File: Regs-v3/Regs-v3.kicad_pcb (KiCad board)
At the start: 2 copper layers, 149.9 x 99.1 mm, 16 parts, among them U1 REG_CNT, U10 REG_CNT, U2 REG_CNT, U3 REG_CNT, U4 REG_CNT, U5 REG_CNT, U6 REG_CNT, U7 REG_CNT, U8 REG_CNT, U9 REG_CNT

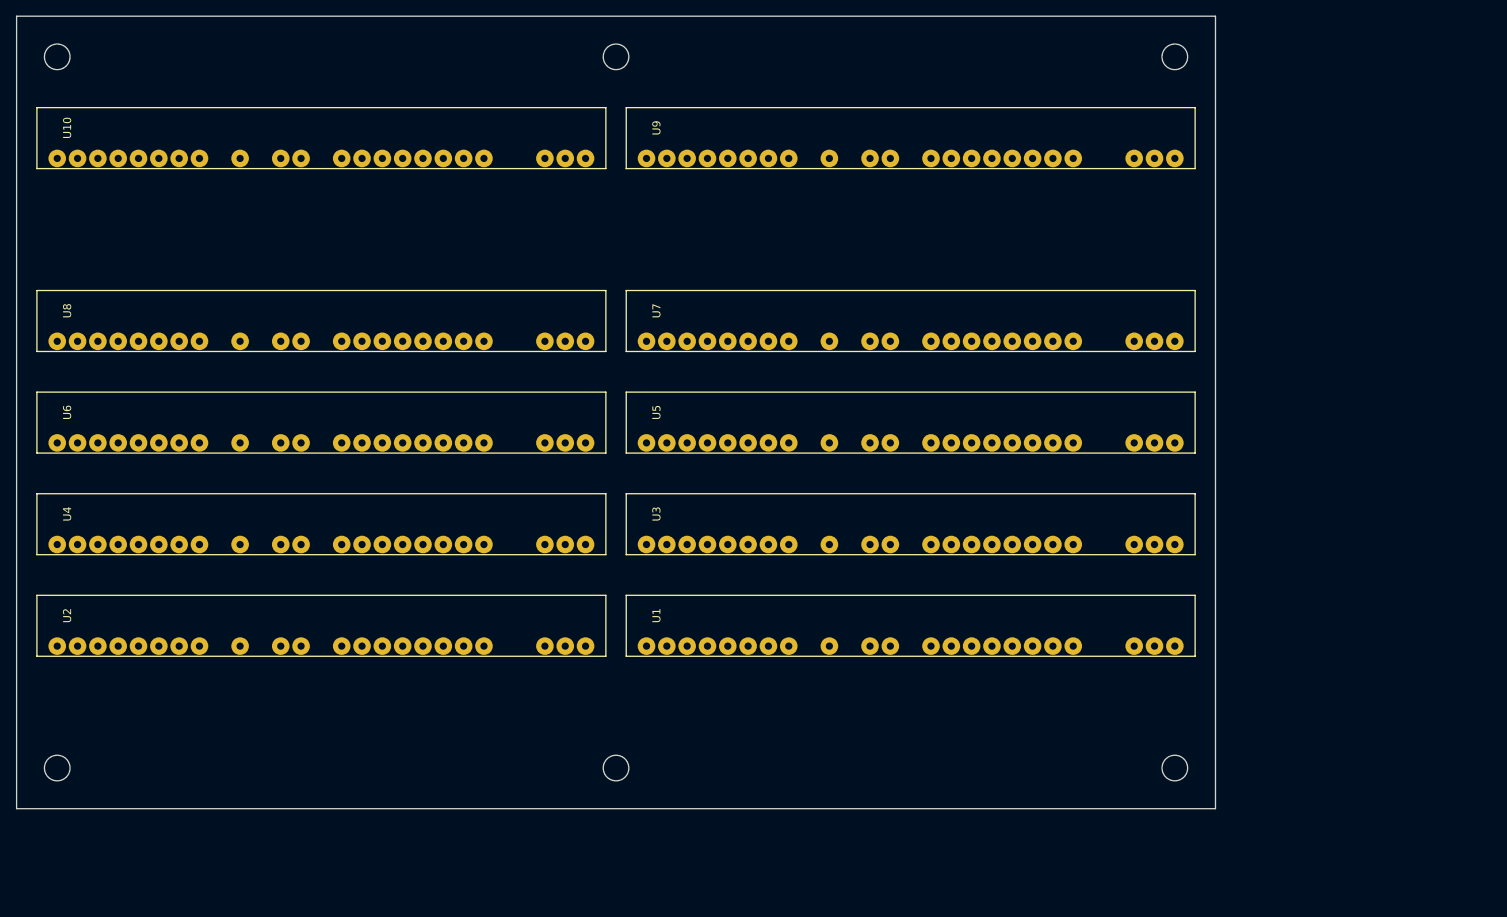
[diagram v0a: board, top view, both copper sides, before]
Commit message: Regs pcb in work
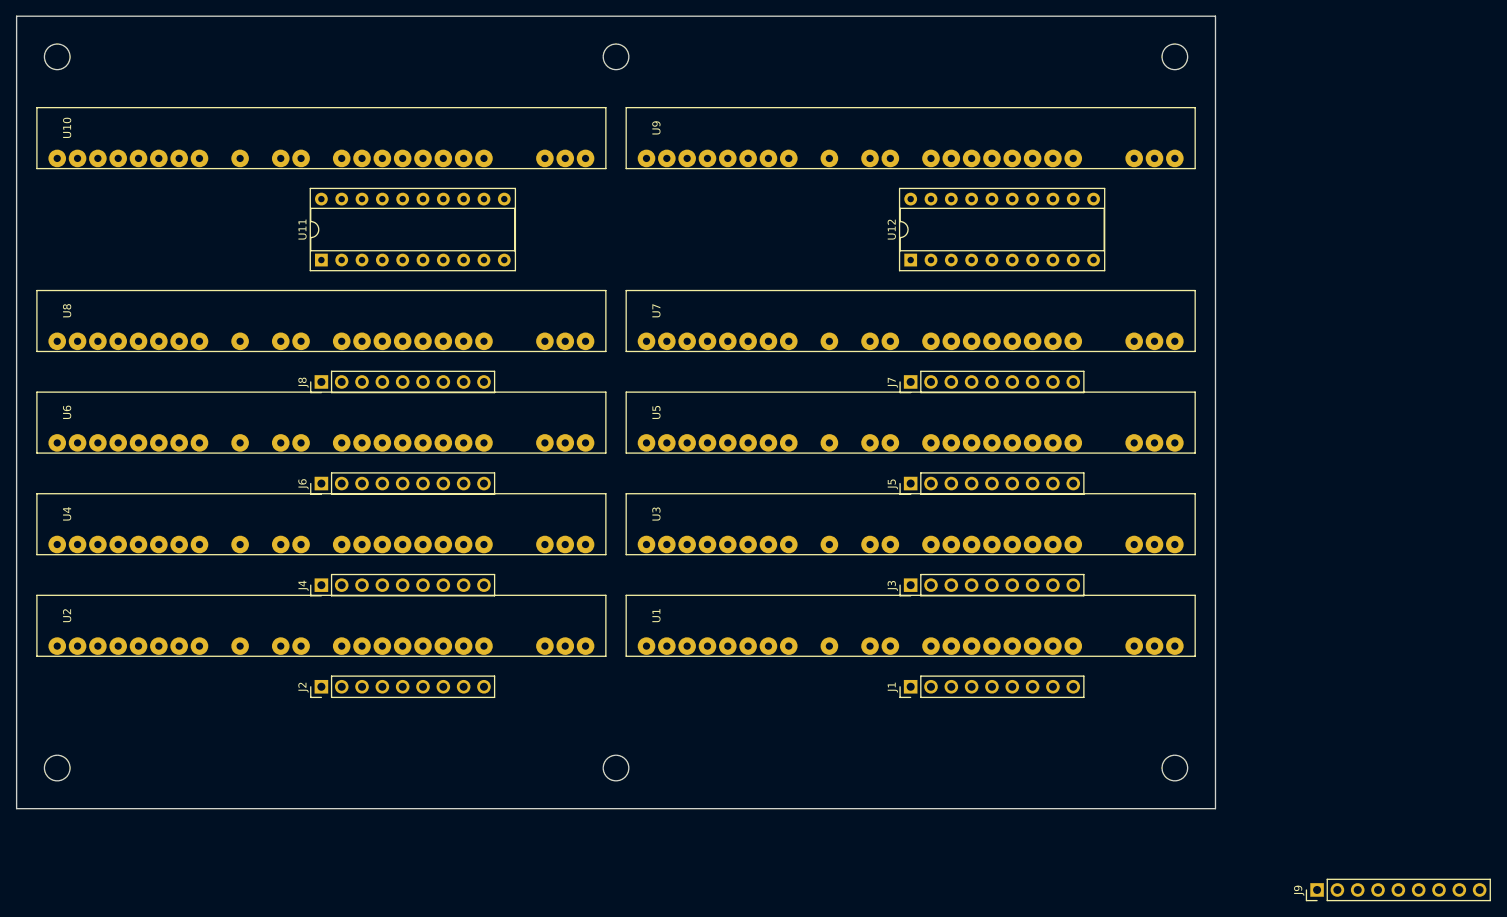
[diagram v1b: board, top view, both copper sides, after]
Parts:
- added J1: Conn_01x09_Male, Connector_PinHeader_2.54mm:PinHeader_1x09_P2.54mm_Vertical, F.Cu at (127.0, 99.1)
- added J2: Conn_01x09_Male, Connector_PinHeader_2.54mm:PinHeader_1x09_P2.54mm_Vertical, F.Cu at (53.3, 99.1)
- added J3: Conn_01x09_Male, Connector_PinHeader_2.54mm:PinHeader_1x09_P2.54mm_Vertical, F.Cu at (127.0, 86.4)
- added J4: Conn_01x09_Male, Connector_PinHeader_2.54mm:PinHeader_1x09_P2.54mm_Vertical, F.Cu at (53.3, 86.4)
- added J5: Conn_01x09_Male, Connector_PinHeader_2.54mm:PinHeader_1x09_P2.54mm_Vertical, F.Cu at (127.0, 73.7)
- added J6: Conn_01x09_Male, Connector_PinHeader_2.54mm:PinHeader_1x09_P2.54mm_Vertical, F.Cu at (53.3, 73.7)
- added J7: Conn_01x09_Male, Connector_PinHeader_2.54mm:PinHeader_1x09_P2.54mm_Vertical, F.Cu at (127.0, 61.0)
- added J8: Conn_01x09_Male, Connector_PinHeader_2.54mm:PinHeader_1x09_P2.54mm_Vertical, F.Cu at (53.3, 61.0)
- added J9: Conn_01x09_Male, Connector_PinHeader_2.54mm:PinHeader_1x09_P2.54mm_Vertical, F.Cu at (177.8, 124.5)
- added U11: 74HC245, Package_DIP:DIP-20_W7.62mm_Socket, F.Cu at (53.3, 45.7)
- added U12: 74HC245, Package_DIP:DIP-20_W7.62mm_Socket, F.Cu at (127.0, 45.7)
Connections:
- net Net-(U10-Pad12) renamed /SPH.0
- net Net-(U10-Pad13) renamed /SPH.1
- net Net-(U10-Pad14) renamed /SPH.2
- net Net-(U10-Pad15) renamed /SPH.3
- net Net-(U10-Pad16) renamed /SPH.4
- net Net-(U10-Pad17) renamed /SPH.5
- net Net-(U10-Pad18) renamed /SPH.6
- net Net-(U10-Pad19) renamed /SPH.7
- net Net-(U9-Pad12) renamed /SPL.0
- net Net-(U9-Pad13) renamed /SPL.1
- net Net-(U9-Pad14) renamed /SPL.2
- net Net-(U9-Pad15) renamed /SPL.3
- net Net-(U9-Pad16) renamed /SPL.4
- net Net-(U9-Pad17) renamed /SPL.5
- net Net-(U9-Pad18) renamed /SPL.6
- net Net-(U9-Pad19) renamed /SPL.7
- U1 pad 10: Net-(U1-Pad10) -> GND
- U1 pad 12: Net-(U1-Pad12) -> /R0.0
- U1 pad 13: Net-(U1-Pad13) -> /R0.1
- U1 pad 14: Net-(U1-Pad14) -> /R0.2
- U1 pad 15: Net-(U1-Pad15) -> /R0.3
- U1 pad 16: Net-(U1-Pad16) -> /R0.4
- U1 pad 17: Net-(U1-Pad17) -> /R0.5
- U1 pad 18: Net-(U1-Pad18) -> /R0.6
- U1 pad 19: Net-(U1-Pad19) -> /R0.7
- U10 pad 10: Net-(U10-Pad10) -> GND
- U2 pad 10: Net-(U2-Pad10) -> GND
- U2 pad 12: Net-(U2-Pad12) -> /R1.0
- U2 pad 13: Net-(U2-Pad13) -> /R1.1
- U2 pad 14: Net-(U2-Pad14) -> /R1.2
- U2 pad 15: Net-(U2-Pad15) -> /R1.3
- U2 pad 16: Net-(U2-Pad16) -> /R1.4
- U2 pad 17: Net-(U2-Pad17) -> /R1.5
- U2 pad 18: Net-(U2-Pad18) -> /R1.6
- U2 pad 19: Net-(U2-Pad19) -> /R1.7
- U3 pad 10: Net-(U3-Pad10) -> GND
- U3 pad 12: Net-(U3-Pad12) -> /R2.0
- U3 pad 13: Net-(U3-Pad13) -> /R2.1
- U3 pad 14: Net-(U3-Pad14) -> /R2.2
- U3 pad 15: Net-(U3-Pad15) -> /R2.3
- U3 pad 16: Net-(U3-Pad16) -> /R2.4
- U3 pad 17: Net-(U3-Pad17) -> /R2.5
- U3 pad 18: Net-(U3-Pad18) -> /R2.6
- U3 pad 19: Net-(U3-Pad19) -> /R2.7
- U4 pad 10: Net-(U4-Pad10) -> GND
- U4 pad 12: Net-(U4-Pad12) -> /R3.0
- U4 pad 13: Net-(U4-Pad13) -> /R3.1
- U4 pad 14: Net-(U4-Pad14) -> /R3.2
- U4 pad 15: Net-(U4-Pad15) -> /R3.3
- U4 pad 16: Net-(U4-Pad16) -> /R3.4
- U4 pad 17: Net-(U4-Pad17) -> /R3.5
- U4 pad 18: Net-(U4-Pad18) -> /R3.6
- U4 pad 19: Net-(U4-Pad19) -> /R3.7
- U5 pad 10: Net-(U5-Pad10) -> GND
- U5 pad 12: Net-(U5-Pad12) -> /R4.0
- U5 pad 13: Net-(U5-Pad13) -> /R4.1
- U5 pad 14: Net-(U5-Pad14) -> /R4.2
- U5 pad 15: Net-(U5-Pad15) -> /R4.3
- U5 pad 16: Net-(U5-Pad16) -> /R4.4
- U5 pad 17: Net-(U5-Pad17) -> /R4.5
- U5 pad 18: Net-(U5-Pad18) -> /R4.6
- U5 pad 19: Net-(U5-Pad19) -> /R4.7
- U6 pad 10: Net-(U6-Pad10) -> GND
- U6 pad 12: Net-(U6-Pad12) -> /R5.0
- U6 pad 13: Net-(U6-Pad13) -> /R5.1
- U6 pad 14: Net-(U6-Pad14) -> /R5.2
- U6 pad 15: Net-(U6-Pad15) -> /R5.3
- U6 pad 16: Net-(U6-Pad16) -> /R5.4
- U6 pad 17: Net-(U6-Pad17) -> /R5.5
- U6 pad 18: Net-(U6-Pad18) -> /R5.6
- U6 pad 19: Net-(U6-Pad19) -> /R5.7
- U7 pad 10: Net-(U7-Pad10) -> GND
- U7 pad 12: Net-(U7-Pad12) -> /R6.0
- U7 pad 13: Net-(U7-Pad13) -> /R6.1
- U7 pad 14: Net-(U7-Pad14) -> /R6.2
- U7 pad 15: Net-(U7-Pad15) -> /R6.3
- U7 pad 16: Net-(U7-Pad16) -> /R6.4
- U7 pad 17: Net-(U7-Pad17) -> /R6.5
- U7 pad 18: Net-(U7-Pad18) -> /R6.6
- U7 pad 19: Net-(U7-Pad19) -> /R6.7
- U8 pad 10: Net-(U8-Pad10) -> GND
- U8 pad 12: Net-(U8-Pad12) -> /R7.0
- U8 pad 13: Net-(U8-Pad13) -> /R7.1
- U8 pad 14: Net-(U8-Pad14) -> /R7.2
- U8 pad 15: Net-(U8-Pad15) -> /R7.3
- U8 pad 16: Net-(U8-Pad16) -> /R7.4
- U8 pad 17: Net-(U8-Pad17) -> /R7.5
- U8 pad 18: Net-(U8-Pad18) -> /R7.6
- U8 pad 19: Net-(U8-Pad19) -> /R7.7
- U9 pad 10: Net-(U9-Pad10) -> GND

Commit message: Regs pcb in work
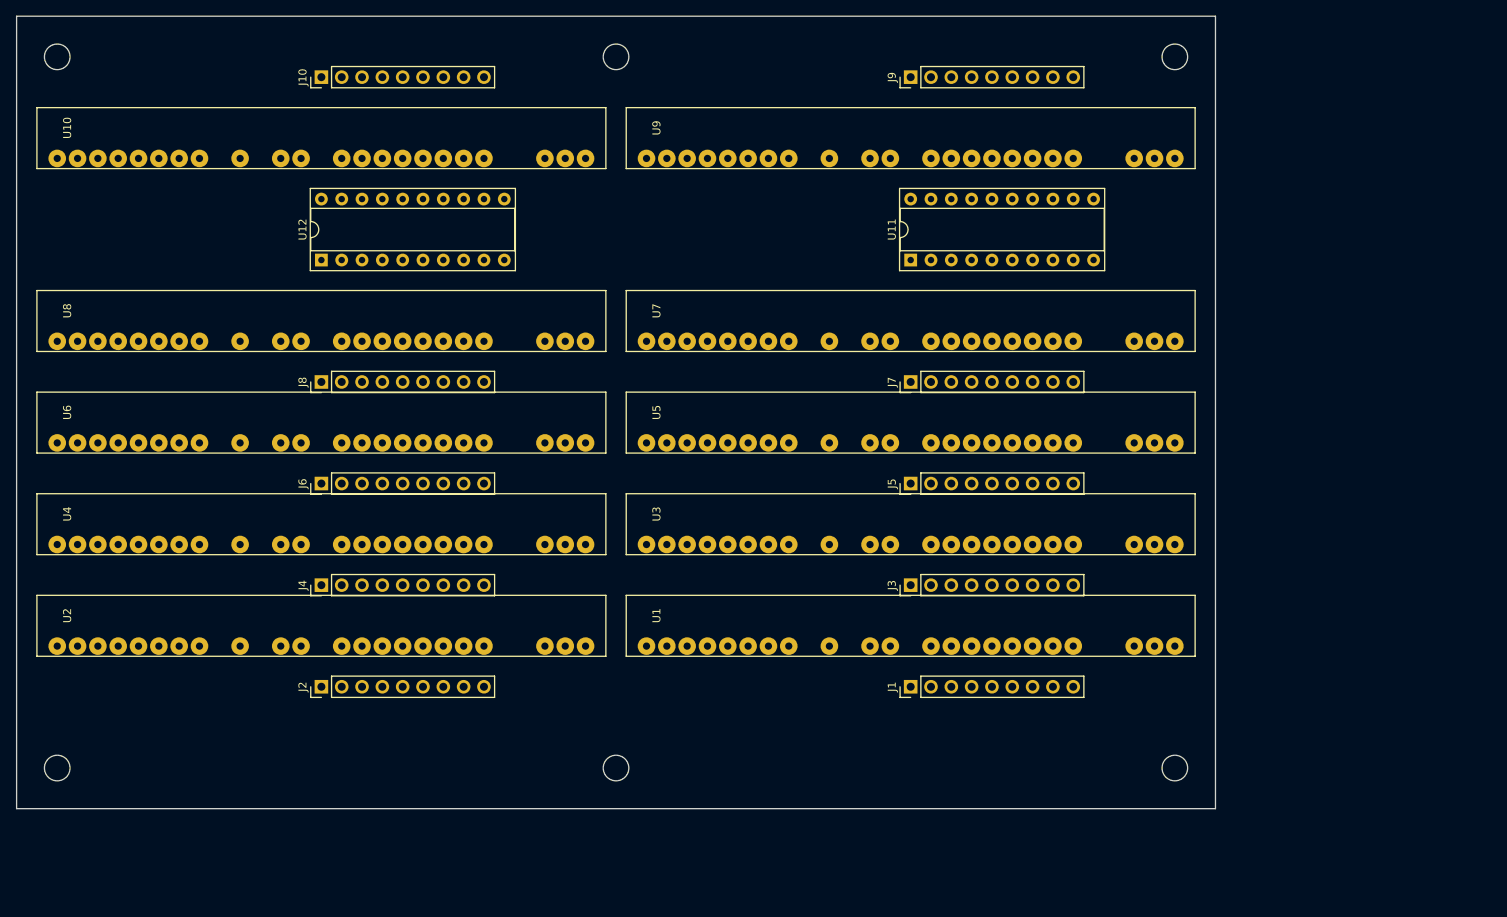
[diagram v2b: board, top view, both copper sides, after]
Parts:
- added J10: Conn_01x09_Male, Connector_PinHeader_2.54mm:PinHeader_1x09_P2.54mm_Vertical, F.Cu at (53.3, 22.9)
- moved J9 113.6 mm to (127.0, 22.9)
- moved U11 73.7 mm to (127.0, 45.7)
- moved U12 73.7 mm to (53.3, 45.7)
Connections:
- J9 pad 2: Net-(J9-Pad2) -> /YL|SPL.0
- J9 pad 3: Net-(J9-Pad3) -> /YL|SPL.1
- J9 pad 4: Net-(J9-Pad4) -> /YL|SPL.2
- J9 pad 5: Net-(J9-Pad5) -> /YL|SPL.3
- J9 pad 6: Net-(J9-Pad6) -> /YL|SPL.4
- J9 pad 7: Net-(J9-Pad7) -> /YL|SPL.5
- J9 pad 8: Net-(J9-Pad8) -> /YL|SPL.6
- J9 pad 9: Net-(J9-Pad9) -> /YL|SPL.7
- U1 pad 11: Net-(U1-Pad11) -> VCC
- U1 pad 20: Net-(U1-Pad20) -> GND
- U10 pad 11: Net-(U10-Pad11) -> VCC
- U10 pad 12: /SPH.0 -> /YH|SPH.0
- U10 pad 13: /SPH.1 -> /YH|SPH.1
- U10 pad 14: /SPH.2 -> /YH|SPH.2
- U10 pad 15: /SPH.3 -> /YH|SPH.3
- U10 pad 16: /SPH.4 -> /YH|SPH.4
- U10 pad 17: /SPH.5 -> /YH|SPH.5
- U10 pad 18: /SPH.6 -> /YH|SPH.6
- U10 pad 19: /SPH.7 -> /YH|SPH.7
- U11 pad 11: Net-(U11-Pad11) -> /YL|SPL.7
- U11 pad 12: Net-(U11-Pad12) -> /YL|SPL.6
- U11 pad 13: Net-(U11-Pad13) -> /YL|SPL.5
- U11 pad 14: Net-(U11-Pad14) -> /YL|SPL.4
- U11 pad 15: Net-(U11-Pad15) -> /YL|SPL.3
- U11 pad 16: Net-(U11-Pad16) -> /YL|SPL.2
- U11 pad 17: Net-(U11-Pad17) -> /YL|SPL.1
- U11 pad 18: Net-(U11-Pad18) -> /YL|SPL.0
- U11 pad 2: Net-(U11-Pad2) -> /R6.0
- U11 pad 20: Net-(U11-Pad20) -> VCC
- U11 pad 3: Net-(U11-Pad3) -> /R6.1
- U11 pad 4: Net-(U11-Pad4) -> /R6.2
- U11 pad 5: Net-(U11-Pad5) -> /R6.3
- U11 pad 6: Net-(U11-Pad6) -> /R6.4
- U11 pad 7: Net-(U11-Pad7) -> /R6.5
- U11 pad 8: Net-(U11-Pad8) -> /R6.6
- U11 pad 9: Net-(U11-Pad9) -> /R6.7
- U12 pad 11: Net-(U12-Pad11) -> /YH|SPH.7
- U12 pad 12: Net-(U12-Pad12) -> /YH|SPH.6
- U12 pad 13: Net-(U12-Pad13) -> /YH|SPH.5
- U12 pad 14: Net-(U12-Pad14) -> /YH|SPH.4
- U12 pad 15: Net-(U12-Pad15) -> /YH|SPH.3
- U12 pad 16: Net-(U12-Pad16) -> /YH|SPH.2
- U12 pad 17: Net-(U12-Pad17) -> /YH|SPH.1
- U12 pad 18: Net-(U12-Pad18) -> /YH|SPH.0
- U12 pad 2: Net-(U12-Pad2) -> /R7.0
- U12 pad 20: Net-(U12-Pad20) -> VCC
- U12 pad 3: Net-(U12-Pad3) -> /R7.1
- U12 pad 4: Net-(U12-Pad4) -> /R7.2
- U12 pad 5: Net-(U12-Pad5) -> /R7.3
- U12 pad 6: Net-(U12-Pad6) -> /R7.4
- U12 pad 7: Net-(U12-Pad7) -> /R7.5
- U12 pad 8: Net-(U12-Pad8) -> /R7.6
- U12 pad 9: Net-(U12-Pad9) -> /R7.7
- U2 pad 11: Net-(U2-Pad11) -> VCC
- U2 pad 20: Net-(U2-Pad20) -> GND
- U3 pad 11: Net-(U3-Pad11) -> VCC
- U3 pad 20: Net-(U3-Pad20) -> GND
- U4 pad 11: Net-(U4-Pad11) -> VCC
- U4 pad 20: Net-(U4-Pad20) -> GND
- U5 pad 11: Net-(U5-Pad11) -> VCC
- U5 pad 20: Net-(U5-Pad20) -> GND
- U6 pad 11: Net-(U6-Pad11) -> VCC
- U6 pad 20: Net-(U6-Pad20) -> GND
- U7 pad 11: Net-(U7-Pad11) -> VCC
- U7 pad 20: Net-(U7-Pad20) -> GND
- U8 pad 11: Net-(U8-Pad11) -> VCC
- U8 pad 20: Net-(U8-Pad20) -> GND
- U9 pad 11: Net-(U9-Pad11) -> VCC
- U9 pad 12: /SPL.0 -> /YL|SPL.0
- U9 pad 13: /SPL.1 -> /YL|SPL.1
- U9 pad 14: /SPL.2 -> /YL|SPL.2
- U9 pad 15: /SPL.3 -> /YL|SPL.3
- U9 pad 16: /SPL.4 -> /YL|SPL.4
- U9 pad 17: /SPL.5 -> /YL|SPL.5
- U9 pad 18: /SPL.6 -> /YL|SPL.6
- U9 pad 19: /SPL.7 -> /YL|SPL.7

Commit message: Regs pcb is almost ready
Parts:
- added J11: Conn_01x03_Male, Connector_PinHeader_2.54mm:PinHeader_1x03_P2.54mm_Vertical, F.Cu at (20.3, 48.3)
- added J12: Conn_01x01_Male, Connector_PinHeader_2.54mm:PinHeader_1x01_P2.54mm_Vertical, F.Cu at (27.9, 35.6)
- added J13: Conn_01x01_Male, Connector_PinHeader_2.54mm:PinHeader_1x01_P2.54mm_Vertical, F.Cu at (116.8, 101.6)
- added J14: Conn_01x01_Male, Connector_PinHeader_2.54mm:PinHeader_1x01_P2.54mm_Vertical, F.Cu at (96.5, 35.6)
- added J15: Conn_01x01_Male, Connector_PinHeader_2.54mm:PinHeader_1x01_P2.54mm_Vertical, F.Cu at (96.5, 48.3)
- added J16: Screw_Terminal_01x02, TerminalBlock_Phoenix:TerminalBlock_Phoenix_MKDS-1,5-2_1x02_P5.00mm_Horizontal, F.Cu at (76.2, 109.2)
- added R1: 10k, Resistor_SMD:R_0805_2012Metric_Pad1.20x1.40mm_HandSolder, B.Cu at (157.5, 37.1)
- added R2: 10k, Resistor_SMD:R_0805_2012Metric_Pad1.20x1.40mm_HandSolder, B.Cu at (86.4, 37.1)
- added R3: 10k, Resistor_SMD:R_0805_2012Metric_Pad1.20x1.40mm_HandSolder, B.Cu at (127.0, 41.6)
- added R4: 10k, Resistor_SMD:R_0805_2012Metric_Pad1.20x1.40mm_HandSolder, B.Cu at (53.3, 41.6)
- added U13: 74LS139, Package_DIP:DIP-16_W7.62mm_Socket, F.Cu at (20.3, 45.7)
- added U14: 74HC00, Package_DIP:DIP-14_W7.62mm_Socket, F.Cu at (94.0, 45.7)
- moved J3 2.54 mm to (127.0, 88.9)
- moved J4 2.54 mm to (53.3, 88.9)
- moved J5 2.54 mm to (127.0, 76.2)
- moved J6 2.54 mm to (53.3, 76.2)
- moved U5 2.54 mm to (94.0, 71.1)
- moved U6 2.54 mm to (20.3, 71.1)
- moved U10 2.54 mm to (20.3, 30.5)
- moved U9 2.54 mm to (94.0, 30.5)
- moved J10 2.54 mm to (53.3, 20.3)
- moved J7 2.54 mm to (127.0, 63.5)
- moved J8 2.54 mm to (53.3, 63.5)
- moved J9 2.54 mm to (127.0, 20.3)
- moved U7 2.54 mm to (94.0, 58.4)
- moved U8 2.54 mm to (20.3, 58.4)
- moved J1 2.54 mm to (127.0, 101.6)
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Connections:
- U1 pad 21: Net-(U1-Pad21) -> /~L
- U1 pad 22: Net-(U1-Pad22) -> /~R0
- U1 pad 9: Net-(U1-Pad9) -> /~Res
- U10 pad 1: Net-(U10-Pad1) -> GND
- U10 pad 2: Net-(U10-Pad2) -> GND
- U10 pad 21: Net-(U10-Pad21) -> Net-(R2-Pad1)
- U10 pad 22: Net-(U10-Pad22) -> Net-(R2-Pad1)
- U10 pad 3: Net-(U10-Pad3) -> GND
- U10 pad 4: Net-(U10-Pad4) -> GND
- U10 pad 5: Net-(U10-Pad5) -> GND
- U10 pad 6: Net-(U10-Pad6) -> GND
- U10 pad 7: Net-(U10-Pad7) -> GND
- U10 pad 8: Net-(U10-Pad8) -> GND
- U10 pad 9: Net-(U10-Pad9) -> /~Res
- U11 pad 19: Net-(U11-Pad19) -> /EXT[1]
- U12 pad 19: Net-(U12-Pad19) -> /EXT[1]
- U2 pad 21: Net-(U2-Pad21) -> /~H
- U2 pad 22: Net-(U2-Pad22) -> /~R0
- U2 pad 9: Net-(U2-Pad9) -> /~Res
- U3 pad 21: Net-(U3-Pad21) -> /~L
- U3 pad 22: Net-(U3-Pad22) -> /~R1
- U3 pad 9: Net-(U3-Pad9) -> /~Res
- U4 pad 21: Net-(U4-Pad21) -> /~H
- U4 pad 22: Net-(U4-Pad22) -> /~R1
- U4 pad 9: Net-(U4-Pad9) -> /~Res
- U5 pad 21: Net-(U5-Pad21) -> /~L
- U5 pad 22: Net-(U5-Pad22) -> /~R2
- U5 pad 9: Net-(U5-Pad9) -> /~Res
- U6 pad 21: Net-(U6-Pad21) -> /~H
- U6 pad 22: Net-(U6-Pad22) -> /~R2
- U6 pad 9: Net-(U6-Pad9) -> /~Res
- U7 pad 21: Net-(U7-Pad21) -> /~L
- U7 pad 22: Net-(U7-Pad22) -> /~R3
- U7 pad 9: Net-(U7-Pad9) -> /~Res
- U8 pad 21: Net-(U8-Pad21) -> /~H
- U8 pad 22: Net-(U8-Pad22) -> /~R3
- U8 pad 9: Net-(U8-Pad9) -> /~Res
- U9 pad 1: Net-(U9-Pad1) -> GND
- U9 pad 2: Net-(U9-Pad2) -> GND
- U9 pad 20: Net-(U9-Pad20) -> Net-(U10-Pad20)
- U9 pad 21: Net-(U9-Pad21) -> Net-(R1-Pad1)
- U9 pad 22: Net-(U9-Pad22) -> Net-(R1-Pad1)
- U9 pad 3: Net-(U9-Pad3) -> GND
- U9 pad 4: Net-(U9-Pad4) -> GND
- U9 pad 5: Net-(U9-Pad5) -> GND
- U9 pad 6: Net-(U9-Pad6) -> GND
- U9 pad 7: Net-(U9-Pad7) -> GND
- U9 pad 8: Net-(U9-Pad8) -> GND
- U9 pad 9: Net-(U9-Pad9) -> /~Res
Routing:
- net GND: track 0.00 -> 617.3 mm, vias 0 -> 18
- net VCC: track 0.00 -> 361.7 mm, vias 0 -> 6
- net /~Res: track 0.00 -> 210.8 mm, vias 0 -> 2
- net /~R0: track 0.00 -> 188.0 mm, vias 0 -> 3
- net /~R1: track 0.00 -> 170.5 mm, vias 0 -> 3
- net /~R2: track 0.00 -> 150.8 mm, vias 0 -> 3
- net /~R3: track 0.00 -> 139.3 mm, vias 0 -> 3
- net /~L: track 0.00 -> 109.2 mm, vias 0 -> 2
- net Net-(U10-Pad20): track 0.00 -> 83.8 mm, vias 0 -> 4
- net /EXT[1]: track 0.00 -> 83.8 mm, vias 0 -> 4
- net Net-(U13-Pad9): track 0.00 -> 74.3 mm, vias 0 -> 2
- net /~H: track 0.00 -> 73.7 mm, vias 0 -> 2
- net Net-(U13-Pad10): track 0.00 -> 66.7 mm, vias 0 -> 2
- net /L7: track 0.00 -> 38.1 mm
- net /L6: track 0.00 -> 38.1 mm
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
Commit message: Polishing Regs
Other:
- board text added: "0"
- board text added: "00"
- board text added: "139"
- board text added: "245"
- board text added: "7"
- board text added: "74HCPU"
- board text added: "DST[0:2]"
- board text added: "EXT[1]"
- board text added: "Gnd"
- board text added: "Latch"
- board text added: "R0"
- board text added: "R1"
- board text added: "R2"
- board text added: "R3"
- board text added: "R4"
- board text added: "R5"
- board text added: "R6"
- board text added: "R7"
- board text added: "REGSv3"
- board text added: "SPH"
- board text added: "SPL"
- board text added: "Vcc"
- board text added: "X"
- board text added: "Y"
- board text added: "YH|SPH"
- board text added: "YL|SPL"
- board text added: "~MUL"
- board text added: "~Res"

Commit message: Regs pcb in work
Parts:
- added U15: MUX2-1, CommonLibrary:CMDwoC, F.Cu at (94.0, 104.1)
- moved J16 27.9 mm to (104.1, 109.2)
- moved J4 10.2 mm to (53.3, 78.7)
- moved J2 10.2 mm to (53.3, 91.4)
- moved J6 10.2 mm to (53.3, 66.0)
- moved J8 10.2 mm to (53.3, 53.3)
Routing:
- net VCC: track 361.7 -> 297.2 mm
- net GND: track 617.3 -> 561.3 mm, vias 18 -> 17
- net /R7.7: track 17.8 -> 12.7 mm
- net /R7.6: track 17.8 -> 12.7 mm
- net /R7.5: track 17.8 -> 12.7 mm
- net /R7.4: track 17.8 -> 12.7 mm
- net /R7.3: track 17.8 -> 12.7 mm
- net /R7.2: track 17.8 -> 12.7 mm
- net /R7.1: track 17.8 -> 12.7 mm
- net /R7.0: track 17.8 -> 12.7 mm
- net /~R0: track 188.0 -> 183.5 mm
- net /~R1: track 170.5 -> 167.5 mm
